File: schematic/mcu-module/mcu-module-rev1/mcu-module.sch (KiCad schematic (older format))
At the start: 24 parts, among them P1 MCU1, P2 MICROSD-SDIO-CD, P3 SWD, P4 MCU2, U1 STM32F103RE, X1 32768Hz, X2 8MHz

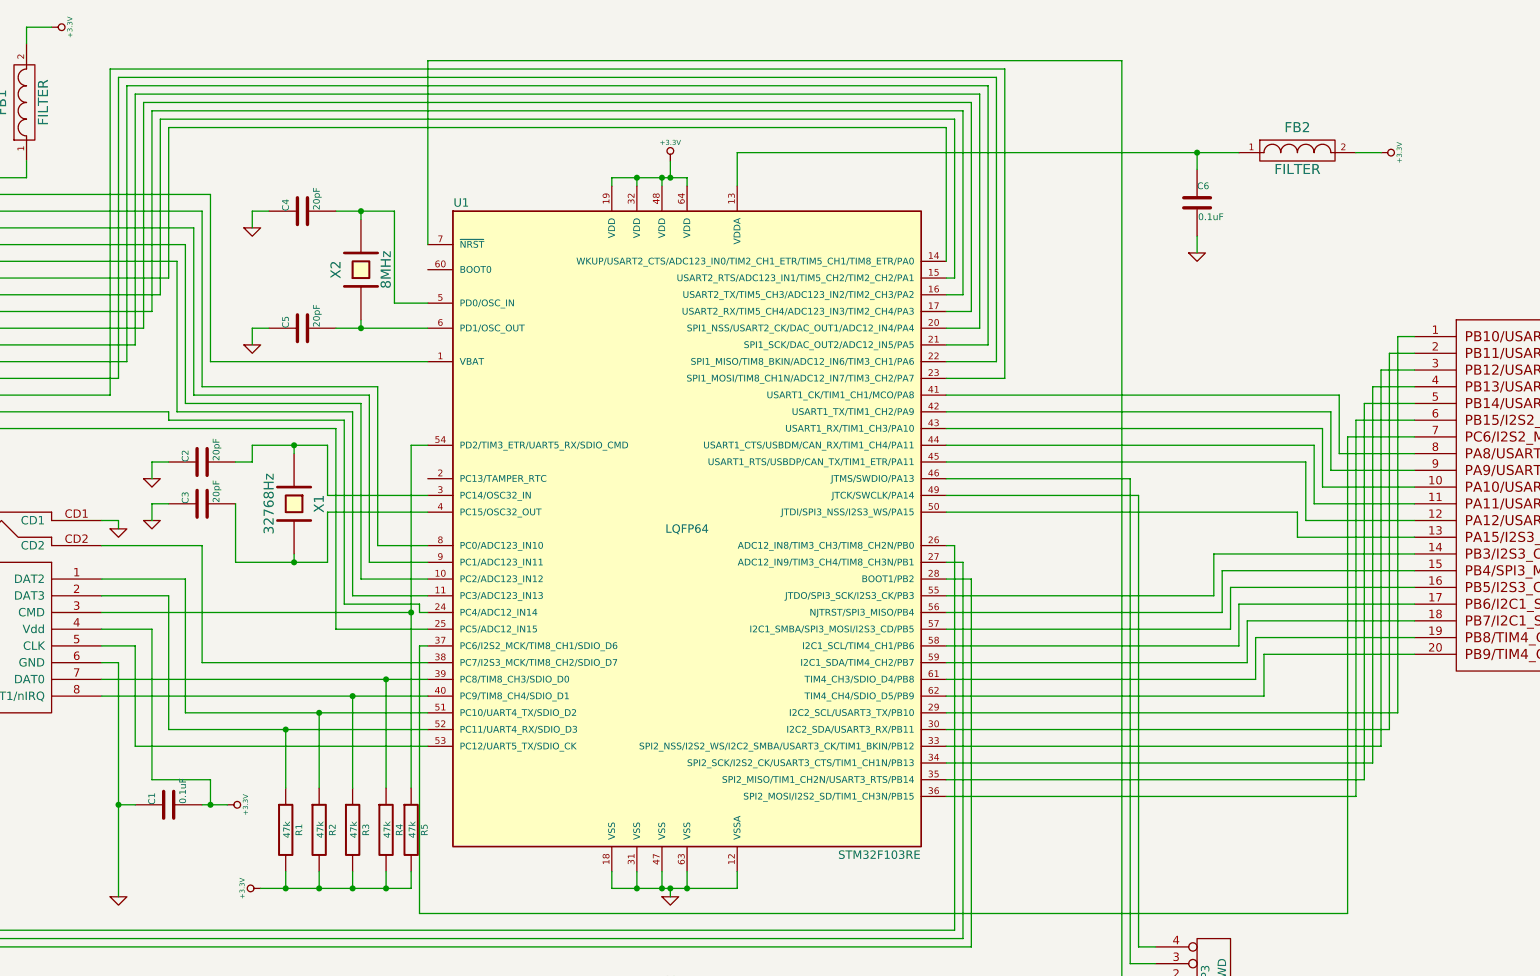
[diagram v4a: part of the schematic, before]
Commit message: New sensor module for LW round plastic sensor; leds are 1206, capacitors fixed
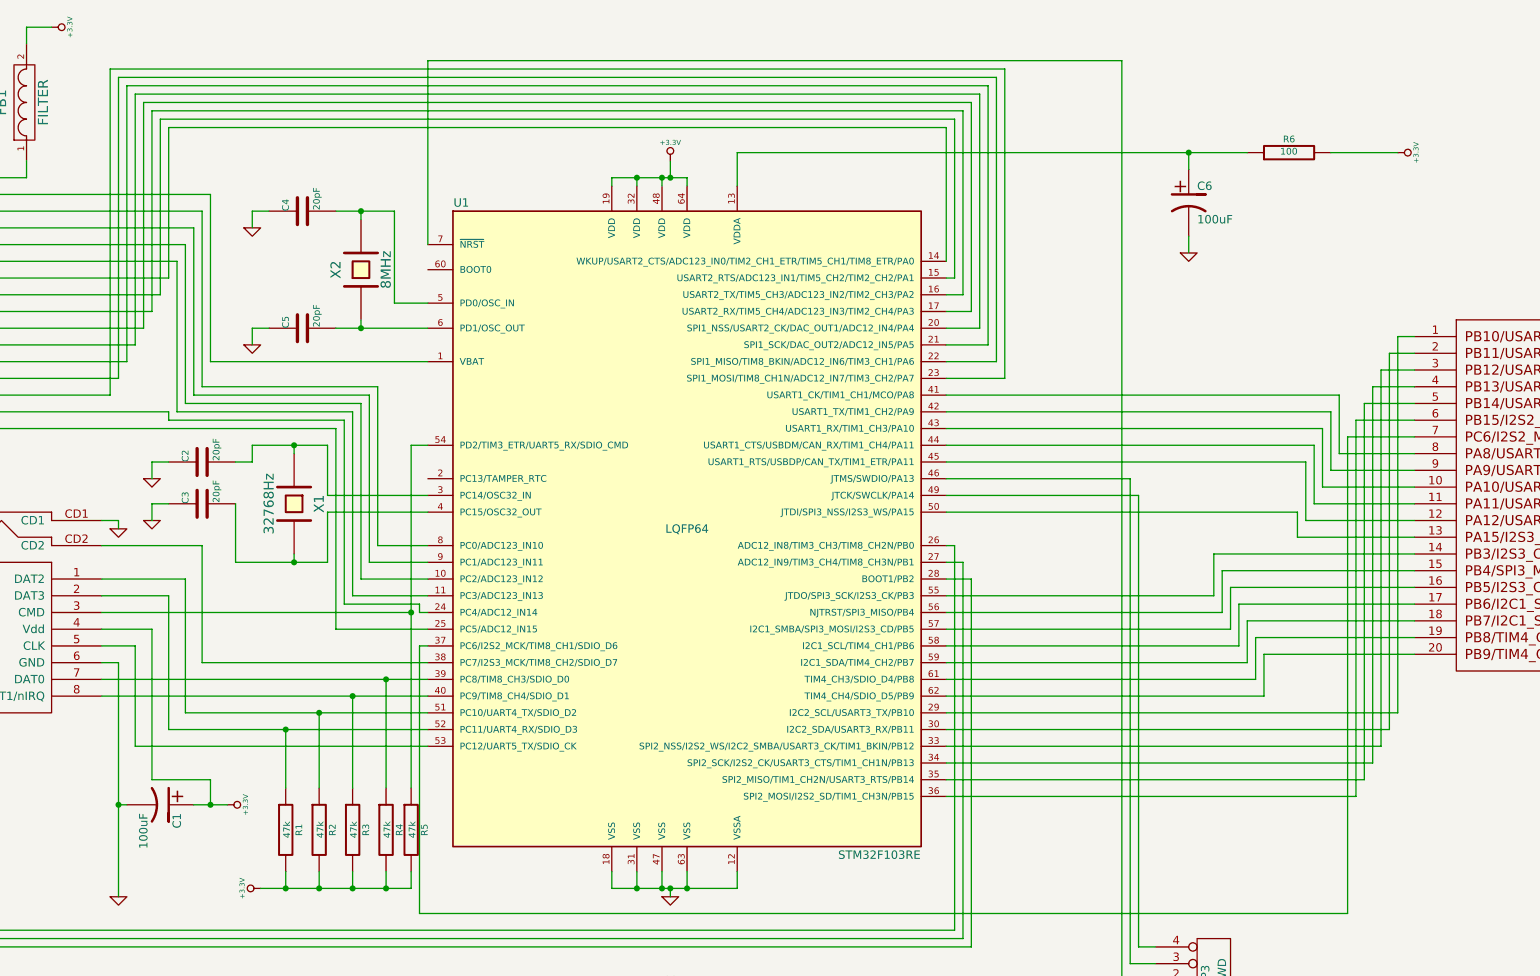
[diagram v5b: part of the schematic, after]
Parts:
- removed C1, C6: 0.1uF, ~, symbol C
- removed FB2: FILTER, ~, symbol FILTER
- added C1, C6: 100uF, ~, symbol CP1
- added R6: 100, ~, symbol R
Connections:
- net +3.3V: now also C1.1, R6.2
- net GND: now also C1.2, C6.2
- net at U1.13 (VDDA): now also C6.1, R6.1
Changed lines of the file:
@@
 Sheet 1 1
 Title "Caustic LT MCU boart"
-Date "24 jan 2016"
+Date "14 apr 2016"
 Rev "1.0"
 Comp ""
@@
 F 3 "" H 8850 4100 60  0000 C CNN
 	1    8850 3800
-	1    0    0    -1
-$EndComp
-$Comp
-L C C6
-U 1 1 55641DCE
-P 11900 1850
-F 0 "C6" H 11900 1950 40  0000 L CNN
-F 1 "0.1uF" H 11906 1765 40  0000 L CNN
-F 2 "~" H 11938 1700 30  0000 C CNN
-F 3 "~" H 11900 1850 60  0000 C CNN
-	1    11900 1850
 	1    0    0    -1
 $EndComp
@@
 $EndComp
 $Comp
-L C C1
-U 1 1 55643130
-P 5750 5450
-F 0 "C1" H 5750 5550 40  0000 L CNN
-F 1 "0.1uF" H 5756 5365 40  0000 L CNN
-F 2 "~" H 5788 5300 30  0000 C CNN
-F 3 "~" H 5750 5450 60  0000 C CNN
-	1    5750 5450
-	0    -1   -1   0
-$EndComp
-$Comp
 L R R1
 U 1 1 5564352C
@@
 Wire Wire Line
 	6000 5300 6000 5450
-Wire Wire Line
-	5950 5450 6100 5450
 Connection ~ 6000 5450
 Connection ~ 5450 5450
@@
 	1    0    0    -1
 $EndComp
-Wire Wire Line
-	5550 5450 5450 5450
 $Comp
 L FILTER FB1
@@
 Connection ~ 8750 7300
 Connection ~ 9050 7300
-$Comp
-L GND #PWR016
-U 1 1 56A481F6
-P 11900 2150
-F 0 "#PWR016" H 11900 2150 30  0001 C CNN
-F 1 "GND" H 11900 2080 30  0001 C CNN
-F 2 "" H 11900 2150 60  0000 C CNN
-F 3 "" H 11900 2150 60  0000 C CNN
-	1    11900 2150
-	1    0    0    -1
-$EndComp
 Wire Wire Line
 	8400 1700 8850 1700
@@
 Connection ~ 8750 1700
 $Comp
-L FILTER FB2
-U 1 1 56A4868A
-P 12500 1550
-F 0 "FB2" H 12500 1700 60  0000 C CNN
-F 1 "FILTER" H 12500 1450 60  0000 C CNN
-F 2 "~" H 12500 1550 60  0000 C CNN
-F 3 "~" H 12500 1550 60  0000 C CNN
-	1    12500 1550
-	1    0    0    -1
-$EndComp
-$Comp
-L +3.3V #PWR017
+L +3.3V #PWR016
 U 1 1 56A48699
-P 13000 1550
-F 0 "#PWR017" H 13000 1510 30  0001 C CNN
-F 1 "+3.3V" H 13000 1660 30  0000 C CNN
-F 2 "" H 13000 1550 60  0000 C CNN
-F 3 "" H 13000 1550 60  0000 C CNN
-	1    13000 1550
+P 13100 1550
+F 0 "#PWR016" H 13100 1510 30  0001 C CNN
+F 1 "+3.3V" H 13100 1660 30  0000 C CNN
+F 2 "" H 13100 1550 60  0000 C CNN
+F 3 "" H 13100 1550 60  0000 C CNN
+	1    13100 1550
 	0    1    1    0
 $EndComp
 Wire Wire Line
-	11900 1650 11900 1550
-Wire Wire Line
-	9150 1550 12150 1550
-Wire Wire Line
-	11900 2050 11900 2150
-Wire Wire Line
-	12850 1550 13000 1550
-Connection ~ 11900 1550
+	9150 1550 12200 1550
+Wire Wire Line
+	12700 1550 13100 1550
+$Comp
+L CP1 C6
+U 1 1 570F5744
+P 11850 1850
+F 0 "C6" H 11900 1950 50  0000 L CNN
+F 1 "100uF" H 11900 1750 50  0000 L CNN
+F 2 "~" H 11850 1850 60  0000 C CNN
+F 3 "~" H 11850 1850 60  0000 C CNN
+	1    11850 1850
+	1    0    0    -1
+$EndComp
+$Comp
+L R R6
+U 1 1 570F5753
+P 12450 1550
+F 0 "R6" V 12530 1550 40  0000 C CNN
+F 1 "100" V 12457 1551 40  0000 C CNN
+F 2 "~" V 12380 1550 30  0000 C CNN
+F 3 "~" H 12450 1550 30  0000 C CNN
+	1    12450 1550
+	0    -1   -1   0
+$EndComp
+Wire Wire Line
+	11850 1650 11850 1550
+Connection ~ 11850 1550
+$Comp
+L GND #PWR017
+U 1 1 570F5AE6
+P 11850 2150
+F 0 "#PWR017" H 11850 2150 30  0001 C CNN
+F 1 "GND" H 11850 2080 30  0001 C CNN
+F 2 "" H 11850 2150 60  0000 C CNN
+F 3 "" H 11850 2150 60  0000 C CNN
+	1    11850 2150
+	1    0    0    -1
+$EndComp
+Wire Wire Line
+	11850 2050 11850 2150
+$Comp
+L CP1 C1
+U 1 1 570F5C31
+P 5700 5450
+F 0 "C1" H 5750 5550 50  0000 L CNN
+F 1 "100uF" H 5750 5350 50  0000 L CNN
+F 2 "~" H 5700 5450 60  0000 C CNN
+F 3 "~" H 5700 5450 60  0000 C CNN
+	1    5700 5450
+	0    1    1    0
+$EndComp
+Wire Wire Line
+	5450 5450 5500 5450
+Wire Wire Line
+	5900 5450 6100 5450
 $EndSCHEMATC
